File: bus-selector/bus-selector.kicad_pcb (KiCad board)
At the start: 2 copper layers, 129.5 x 63.5 mm, 223 parts, among them J1 Conn_01x08, J2 Conn_01x08, J3 Conn_01x08, J4 Conn_01x08, J5 Conn_01x02, J6 Conn_01x08, J7 PWR-2_pole_power_connector, Q1 2N7000, Q10 2N7000, Q11 2N7000, Q12 2N7000, Q13 2N7000, Q14 2N7000, Q15 2N7000, Q16 2N7000, Q17 2N7000, Q18 2N7000, Q19 2N7000, Q2 2N7000, Q20 2N7000, Q21 2N7000, Q22 2N7000, Q23 2N7000, Q24 2N7000, Q25 2N7000, Q26 2N7000, Q27 2N7000, Q28 2N7000, Q29 2N7000, Q3 2N7000, Q30 2N7000, Q31 2N7000, Q32 2N7000, Q33 2N7000, Q34 2N7000, Q35 2N7000, Q36 2N7000, Q37 2N7000, Q38 2N7000, Q39 2N7000, Q4 2N7000, Q40 2N7000, Q41 2N7000, Q42 2N7000, Q43 2N7000, Q44 2N7000, Q45 2N7000, Q46 2N7000, Q47 2N7000, Q48 2N7000, Q49 2N7000, Q5 2N7000, Q50 2N7000, Q51 2N7000, Q52 2N7000, Q53 2N7000, Q54 2N7000, Q55 2N7000, Q56 2N7000, Q57 2N7000, Q58 2N7000, Q59 2N7000, Q6 2N7000, Q60 2N7000, Q61 2N7000, Q62 2N7000, Q63 2N7000, Q64 2N7000, Q65 2N7000, Q66 2N7000, Q67 2N7000, Q68 2N7000, Q69 2N7000, Q7 2N7000, Q70 2N7000, Q71 2N7000, Q72 2N7000, Q73 2N7000, Q74 2N7000, Q75 2N7000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

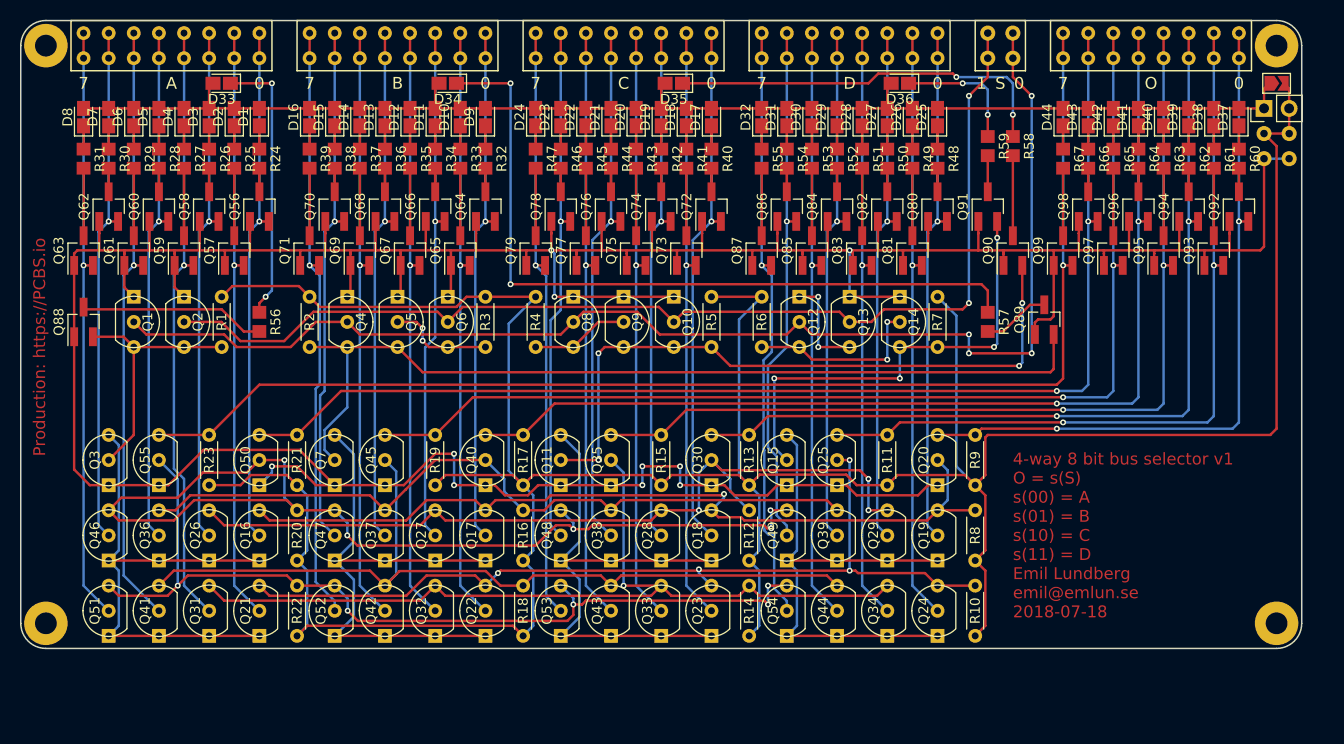
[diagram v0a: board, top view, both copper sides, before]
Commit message: Add pull-down resistors to bus selector inputs
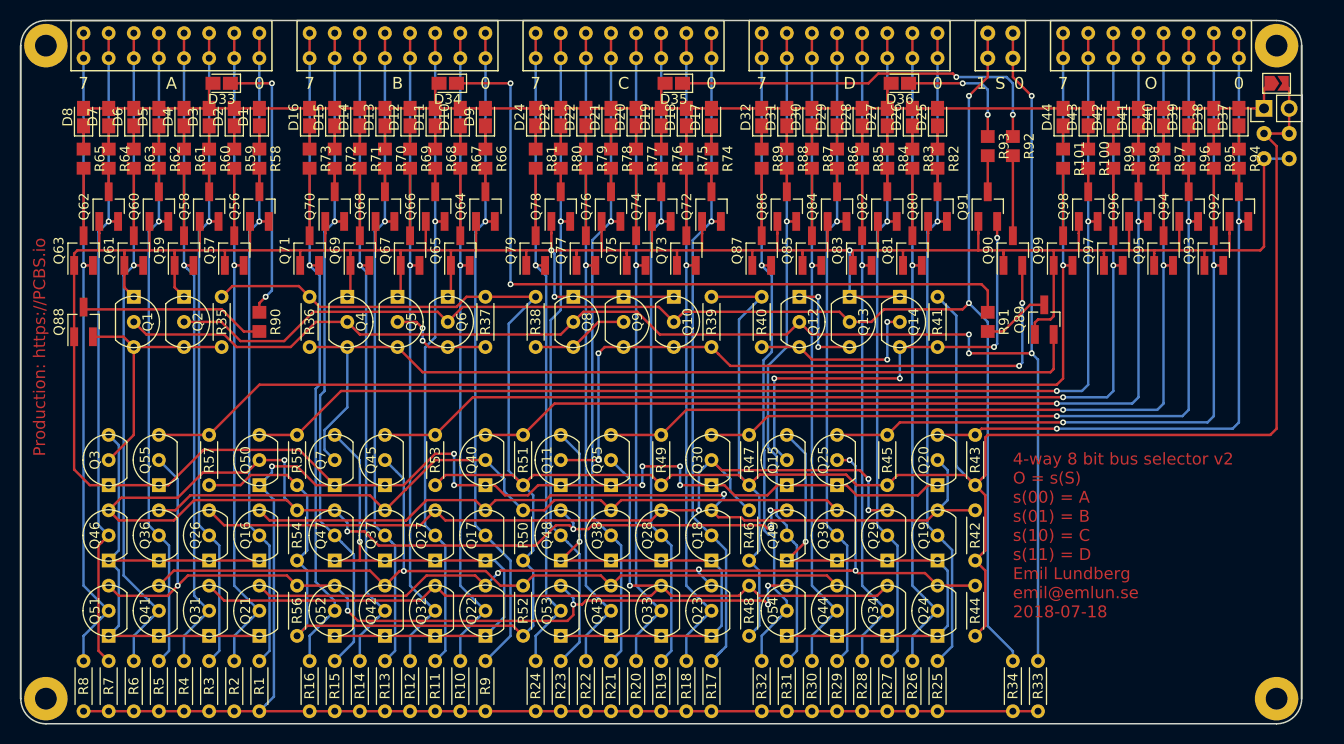
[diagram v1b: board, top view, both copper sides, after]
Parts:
- removed the REF** at (146.1, 77.5)
- removed the REF** at (21.6, 77.5)
- added R100: R, Resistor_SMD:R_0805_2012Metric_Pad1.29x1.40mm_HandSolder, F.Cu at (127.0, 30.5)
- added R101: R, Resistor_SMD:R_0805_2012Metric_Pad1.29x1.40mm_HandSolder, F.Cu at (124.5, 30.5)
- added R68: R, Resistor_SMD:R_0805_2012Metric_Pad1.29x1.40mm_HandSolder, F.Cu at (61.0, 30.5)
- added R69: R, Resistor_SMD:R_0805_2012Metric_Pad1.29x1.40mm_HandSolder, F.Cu at (58.4, 30.5)
- added R70: R, Resistor_SMD:R_0805_2012Metric_Pad1.29x1.40mm_HandSolder, F.Cu at (55.9, 30.5)
- added R71: R, Resistor_SMD:R_0805_2012Metric_Pad1.29x1.40mm_HandSolder, F.Cu at (53.3, 30.5)
- added R72: R, Resistor_SMD:R_0805_2012Metric_Pad1.29x1.40mm_HandSolder, F.Cu at (50.8, 30.5)
- added R73: R, Resistor_SMD:R_0805_2012Metric_Pad1.29x1.40mm_HandSolder, F.Cu at (48.3, 30.5)
- added R74: R, Resistor_SMD:R_0805_2012Metric_Pad1.29x1.40mm_HandSolder, F.Cu at (88.9, 30.5)
- added R75: R, Resistor_SMD:R_0805_2012Metric_Pad1.29x1.40mm_HandSolder, F.Cu at (86.4, 30.5)
- added R76: R, Resistor_SMD:R_0805_2012Metric_Pad1.29x1.40mm_HandSolder, F.Cu at (83.8, 30.5)
- added R77: R, Resistor_SMD:R_0805_2012Metric_Pad1.29x1.40mm_HandSolder, F.Cu at (81.3, 30.5)
- added R78: R, Resistor_SMD:R_0805_2012Metric_Pad1.29x1.40mm_HandSolder, F.Cu at (78.7, 30.5)
- added R79: R, Resistor_SMD:R_0805_2012Metric_Pad1.29x1.40mm_HandSolder, F.Cu at (76.2, 30.5)
- added R80: R, Resistor_SMD:R_0805_2012Metric_Pad1.29x1.40mm_HandSolder, F.Cu at (73.7, 30.5)
- added R81: R, Resistor_SMD:R_0805_2012Metric_Pad1.29x1.40mm_HandSolder, F.Cu at (71.1, 30.5)
- added R82: R, Resistor_SMD:R_0805_2012Metric_Pad1.29x1.40mm_HandSolder, F.Cu at (111.8, 30.5)
- added R83: R, Resistor_SMD:R_0805_2012Metric_Pad1.29x1.40mm_HandSolder, F.Cu at (109.2, 30.5)
- added R84: R, Resistor_SMD:R_0805_2012Metric_Pad1.29x1.40mm_HandSolder, F.Cu at (106.7, 30.5)
- added R85: R, Resistor_SMD:R_0805_2012Metric_Pad1.29x1.40mm_HandSolder, F.Cu at (104.1, 30.5)
- added R86: R, Resistor_SMD:R_0805_2012Metric_Pad1.29x1.40mm_HandSolder, F.Cu at (101.6, 30.5)
- added R87: R, Resistor_SMD:R_0805_2012Metric_Pad1.29x1.40mm_HandSolder, F.Cu at (99.1, 30.5)
- added R88: R, Resistor_SMD:R_0805_2012Metric_Pad1.29x1.40mm_HandSolder, F.Cu at (96.5, 30.5)
- added R89: R, Resistor_SMD:R_0805_2012Metric_Pad1.29x1.40mm_HandSolder, F.Cu at (94.0, 30.5)
- added R90: R, Resistor_SMD:R_0805_2012Metric_Pad1.29x1.40mm_HandSolder, F.Cu at (43.2, 47.0)
- added R91: R, Resistor_SMD:R_0805_2012Metric_Pad1.29x1.40mm_HandSolder, F.Cu at (116.8, 47.0)
- added R92: R, Resistor_SMD:R_0805_2012Metric_Pad1.29x1.40mm_HandSolder, F.Cu at (119.4, 29.2)
- added R93: R, Resistor_SMD:R_0805_2012Metric_Pad1.29x1.40mm_HandSolder, F.Cu at (116.8, 29.2)
- added R94: R, Resistor_SMD:R_0805_2012Metric_Pad1.29x1.40mm_HandSolder, F.Cu at (142.2, 30.5)
- added R95: R, Resistor_SMD:R_0805_2012Metric_Pad1.29x1.40mm_HandSolder, F.Cu at (139.7, 30.5)
- added R96: R, Resistor_SMD:R_0805_2012Metric_Pad1.29x1.40mm_HandSolder, F.Cu at (137.2, 30.5)
- added R97: R, Resistor_SMD:R_0805_2012Metric_Pad1.29x1.40mm_HandSolder, F.Cu at (134.6, 30.5)
- added R98: R, Resistor_SMD:R_0805_2012Metric_Pad1.29x1.40mm_HandSolder, F.Cu at (132.1, 30.5)
- added R99: R, Resistor_SMD:R_0805_2012Metric_Pad1.29x1.40mm_HandSolder, F.Cu at (129.5, 30.5)
- added REF**: MountingHole_2.2mm_M2_Pad, MountingHole:MountingHole_2.2mm_M2_Pad, F.Cu at (146.1, 85.1)
- added REF**: MountingHole_2.2mm_M2_Pad, MountingHole:MountingHole_2.2mm_M2_Pad, F.Cu at (21.6, 85.1)
- R24, R25, R26, R27, R28, R29, R30, R31, R32, R33, R34, R35, R36, R37, R38, R39, R40, R41, R42, R43, R44, R45, R46, R47, R48, R49, R50, R51, R52, R53, R54, R55, R56, R57: footprint Resistor_SMD:R_0805_2012Metric_Pad1.29x1.40mm_HandSolder -> emlun:R_Axial_DIN0204_L3.6mm_D1.6mm_P5.08mm_Horizontal
- moved R60 104.1 mm to (38.1, 30.5)
- moved R64 104.1 mm to (27.9, 30.5)
- moved R63 104.1 mm to (30.5, 30.5)
- moved R61 104.1 mm to (35.6, 30.5)
- moved R62 104.1 mm to (33.0, 30.5)
- moved R65 104.1 mm to (25.4, 30.5)
- moved R7 91.6 mm to (27.9, 81.3)
- moved R8 90.7 mm to (25.4, 81.3), turned to 270 degrees
- moved R25 87.4 mm to (111.8, 81.3)
- moved R26 87.4 mm to (109.2, 81.3)
- moved R27 87.4 mm to (106.7, 81.3)
- moved R28 87.4 mm to (104.1, 81.3)
- moved R30 87.4 mm to (99.1, 81.3)
- moved R31 87.4 mm to (96.5, 81.3)
- moved R29 87.4 mm to (101.6, 81.3)
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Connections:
- R1 pad 1: VCC -> /a0
- R1 pad 2: /sa -> GND
- R10 pad 1: VCC -> /b1
- R10 pad 2: Net-(Q21-Pad3) -> GND
- R11 pad 1: VCC -> /b2
- R11 pad 2: /o1 -> GND
- R12 pad 1: VCC -> /b3
- R12 pad 2: Net-(Q26-Pad3) -> GND
- R13 pad 1: VCC -> /b4
- R13 pad 2: /o2 -> GND
- R14 pad 1: VCC -> /b5
- R14 pad 2: Net-(Q31-Pad3) -> GND
- R15 pad 1: VCC -> /b6
- R15 pad 2: /o3 -> GND
- R16 pad 1: VCC -> /b7
- R16 pad 2: Net-(Q36-Pad3) -> GND
- R17 pad 1: VCC -> /c0
- R17 pad 2: /o4 -> GND
- R18 pad 1: VCC -> /c1
- R18 pad 2: Net-(Q41-Pad3) -> GND
- R19 pad 1: VCC -> /c2
- R19 pad 2: /o5 -> GND
- R2 pad 1: VCC -> /a1
- R2 pad 2: /sb -> GND
- R20 pad 1: VCC -> /c3
- R20 pad 2: Net-(Q46-Pad3) -> GND
- R21 pad 1: VCC -> /c4
- R21 pad 2: /o6 -> GND
- R22 pad 1: VCC -> /c5
- R22 pad 2: Net-(Q51-Pad3) -> GND
- R23 pad 1: VCC -> /c6
- R23 pad 2: /o7 -> GND
- R24 pad 1: Net-(D1-Pad1) -> /c7
- R24 pad 2: Net-(Q56-Pad3) -> GND
- R25 pad 1: Net-(D2-Pad1) -> /d0
- R25 pad 2: Net-(Q57-Pad3) -> GND
- R26 pad 1: Net-(D3-Pad1) -> /d1
- R26 pad 2: Net-(Q58-Pad3) -> GND
- R27 pad 1: Net-(D4-Pad1) -> /d2
- R27 pad 2: Net-(Q59-Pad3) -> GND
- R28 pad 1: Net-(D5-Pad1) -> /d3
- R28 pad 2: Net-(Q60-Pad3) -> GND
- R29 pad 1: Net-(D6-Pad1) -> /d4
- R29 pad 2: Net-(Q61-Pad3) -> GND
- R3 pad 1: VCC -> /a2
- R3 pad 2: Net-(Q5-Pad2) -> GND
- R30 pad 1: Net-(D7-Pad1) -> /d5
- R30 pad 2: Net-(Q62-Pad3) -> GND
- R31 pad 1: Net-(D8-Pad1) -> /d6
- R31 pad 2: Net-(Q63-Pad3) -> GND
- R32 pad 1: Net-(D9-Pad1) -> /d7
- R32 pad 2: Net-(Q64-Pad3) -> GND
- R33 pad 1: Net-(D10-Pad1) -> /s0
- R33 pad 2: Net-(Q65-Pad3) -> GND
- R34 pad 1: Net-(D11-Pad1) -> /s1
- R34 pad 2: Net-(Q66-Pad3) -> GND
- R35 pad 1: Net-(D12-Pad1) -> VCC
- R35 pad 2: Net-(Q67-Pad3) -> /sa
- R36 pad 1: Net-(D13-Pad1) -> VCC
- R36 pad 2: Net-(Q68-Pad3) -> /sb
- R37 pad 1: Net-(D14-Pad1) -> VCC
- R37 pad 2: Net-(Q69-Pad3) -> Net-(Q5-Pad2)
- R38 pad 1: Net-(D15-Pad1) -> VCC
- R38 pad 2: Net-(Q70-Pad3) -> Net-(Q8-Pad3)
- R39 pad 1: Net-(D16-Pad1) -> VCC
- R39 pad 2: Net-(Q71-Pad3) -> /sc
- R4 pad 1: VCC -> /a3
- R4 pad 2: Net-(Q8-Pad3) -> GND
- R40 pad 1: Net-(D17-Pad1) -> VCC
- R40 pad 2: Net-(Q72-Pad3) -> Net-(Q12-Pad3)
- R41 pad 1: Net-(D18-Pad1) -> VCC
- R41 pad 2: Net-(Q73-Pad3) -> /sd
- R42 pad 1: Net-(D19-Pad1) -> VCC
- R42 pad 2: Net-(Q74-Pad3) -> Net-(Q16-Pad3)
- R43 pad 1: Net-(D20-Pad1) -> VCC
- R43 pad 2: Net-(Q75-Pad3) -> /o0
- R44 pad 1: Net-(D21-Pad1) -> VCC
- R44 pad 2: Net-(Q76-Pad3) -> Net-(Q21-Pad3)
- R45 pad 1: Net-(D22-Pad1) -> VCC
- R45 pad 2: Net-(Q77-Pad3) -> /o1
- R46 pad 1: Net-(D23-Pad1) -> VCC
- R46 pad 2: Net-(Q78-Pad3) -> Net-(Q26-Pad3)
- R47 pad 1: Net-(D24-Pad1) -> VCC
- R47 pad 2: Net-(Q79-Pad3) -> /o2
- R48 pad 1: Net-(D25-Pad1) -> VCC
- R48 pad 2: Net-(Q80-Pad3) -> Net-(Q31-Pad3)
- R49 pad 1: Net-(D26-Pad1) -> VCC
- R49 pad 2: Net-(Q81-Pad3) -> /o3
- R5 pad 1: VCC -> /a4
- R5 pad 2: /sc -> GND
- R50 pad 1: Net-(D27-Pad1) -> VCC
- R50 pad 2: Net-(Q82-Pad3) -> Net-(Q36-Pad3)
- R51 pad 1: Net-(D28-Pad1) -> VCC
- R51 pad 2: Net-(Q83-Pad3) -> /o4
- R52 pad 1: Net-(D29-Pad1) -> VCC
- R52 pad 2: Net-(Q84-Pad3) -> Net-(Q41-Pad3)
- R53 pad 1: Net-(D30-Pad1) -> VCC
- R53 pad 2: Net-(Q85-Pad3) -> /o5
- R54 pad 1: Net-(D31-Pad1) -> VCC
- R54 pad 2: Net-(Q86-Pad3) -> Net-(Q46-Pad3)
- R55 pad 1: Net-(D32-Pad1) -> VCC
- R55 pad 2: Net-(Q87-Pad3) -> /o6
- R56 pad 1: Net-(D33-Pad1) -> VCC
- R56 pad 2: Net-(Q88-Pad3) -> Net-(Q51-Pad3)
- R57 pad 1: Net-(D34-Pad1) -> VCC
- R57 pad 2: Net-(Q89-Pad3) -> /o7
- R58 pad 1: Net-(D35-Pad1) -> Net-(D1-Pad1)
- R58 pad 2: Net-(Q90-Pad3) -> Net-(Q56-Pad3)
- R59 pad 1: Net-(D36-Pad1) -> Net-(D2-Pad1)
- R59 pad 2: Net-(Q91-Pad3) -> Net-(Q57-Pad3)
- R6 pad 1: VCC -> /a5
- R6 pad 2: Net-(Q12-Pad3) -> GND
- R60 pad 1: Net-(D37-Pad1) -> Net-(D3-Pad1)
- R60 pad 2: Net-(Q92-Pad3) -> Net-(Q58-Pad3)
- R61 pad 1: Net-(D38-Pad1) -> Net-(D4-Pad1)
- R61 pad 2: Net-(Q93-Pad3) -> Net-(Q59-Pad3)
- R62 pad 1: Net-(D39-Pad1) -> Net-(D5-Pad1)
- R62 pad 2: Net-(Q94-Pad3) -> Net-(Q60-Pad3)
- R63 pad 1: Net-(D40-Pad1) -> Net-(D6-Pad1)
- R63 pad 2: Net-(Q95-Pad3) -> Net-(Q61-Pad3)
- R64 pad 1: Net-(D41-Pad1) -> Net-(D7-Pad1)
- R64 pad 2: Net-(Q96-Pad3) -> Net-(Q62-Pad3)
- R65 pad 1: Net-(D42-Pad1) -> Net-(D8-Pad1)
- R65 pad 2: Net-(Q97-Pad3) -> Net-(Q63-Pad3)
- R66 pad 1: Net-(D43-Pad1) -> Net-(D9-Pad1)
- R66 pad 2: Net-(Q98-Pad3) -> Net-(Q64-Pad3)
- R67 pad 1: Net-(D44-Pad1) -> Net-(D10-Pad1)
- R67 pad 2: Net-(Q99-Pad3) -> Net-(Q65-Pad3)
- R7 pad 1: VCC -> /a6
- R7 pad 2: /sd -> GND
- R8 pad 1: VCC -> /a7
- R8 pad 2: Net-(Q16-Pad3) -> GND
- R9 pad 1: VCC -> /b0
- R9 pad 2: /o0 -> GND
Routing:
- net GND: track 409.3 -> 529.9 mm
- net /s1: track 112.8 -> 150.9 mm
- net /s0: track 131.5 -> 162.8 mm
- net /c0: track 53.3 -> 70.1 mm
- net /b0: track 52.6 -> 67.4 mm
- net /b6: track 53.0 -> 67.3 mm
- net /c6: track 52.6 -> 66.9 mm
- net /d0: track 52.6 -> 66.5 mm
- net /d6: track 53.3 -> 66.9 mm
- net /d4: track 52.6 -> 66.1 mm
- net /c4: track 53.3 -> 66.9 mm
- net /c2: track 52.6 -> 66.1 mm
- net /b2: track 52.6 -> 66.1 mm
- net /a0: track 52.6 -> 66.1 mm
- net /b4: track 52.6 -> 66.1 mm
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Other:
- board size 129.5 x 63.5 mm -> 129.5 x 71.1 mm
- board text added: "4-way 8 bit bus selector v2 O = s(S) s(00) = A s(01) = B s(10) = C s(11) = D Emil Lundberg emil@emlun.se 2018-07-18"
- board text removed: "4-way 8 bit bus selector v1 O = s(S) s(00) = A s(01) = B s(10) = C s(11) = D Emil Lundberg emil@emlun.se 2018-07-18"
